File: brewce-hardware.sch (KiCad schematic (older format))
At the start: 18 parts, among them P1 CONN_I, P2 CONN_O, Q1 Q_NMOS_DGS, Q2 Q_NMOS_DGS, Q3 Q_NMOS_DGS, U1 MCP1700-3302E_TO92

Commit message: update schematics & PCB
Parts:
- added P3: CONN_DS18B20, Connect:bornier3, symbol CONN_01X03
- added R10: 4.7k, Resistors_ThroughHole:Resistor_Horizontal_RM10mm, symbol R
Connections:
- net GND: now also P3.1 (P1)
- net VDD: now also P3.3 (P3), R10.2
- new net: P3.2 (P2), R10.1
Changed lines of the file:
@@
 Wire Wire Line
 	2100 3200 2100 3000
+$Comp
+L CONN_01X03 P3
+U 1 1 5A0C64D8
+P 8550 5000
+F 0 "P3" H 8550 5200 50  0000 C CNN
+F 1 "CONN_DS18B20" V 8650 5000 50  0000 C CNN
+F 2 "Connect:bornier3" H 8550 5000 50  0001 C CNN
+F 3 "" H 8550 5000 50  0000 C CNN
+	1    8550 5000
+	1    0    0    1
+$EndComp
+$Comp
+L GND #PWR016
+U 1 1 5A0C682F
+P 8300 5250
+F 0 "#PWR016" H 8300 5000 50  0001 C CNN
+F 1 "GND" H 8300 5100 50  0000 C CNN
+F 2 "" H 8300 5250 50  0001 C CNN
+F 3 "" H 8300 5250 50  0001 C CNN
+	1    8300 5250
+	1    0    0    -1
+$EndComp
+Wire Wire Line
+	8350 5100 8300 5100
+Wire Wire Line
+	8300 5100 8300 5250
+$Comp
+L VDD #PWR017
+U 1 1 5A0C6B13
+P 8300 4500
+F 0 "#PWR017" H 8300 4350 50  0001 C CNN
+F 1 "VDD" H 8300 4650 50  0000 C CNN
+F 2 "" H 8300 4500 50  0001 C CNN
+F 3 "" H 8300 4500 50  0001 C CNN
+	1    8300 4500
+	1    0    0    -1
+$EndComp
+Wire Wire Line
+	8300 4900 8350 4900
+Wire Wire Line
+	8300 4500 8300 4900
+$Comp
+L R R10
+U 1 1 5A0C6C12
+P 8100 4800
+F 0 "R10" V 8180 4800 50  0000 C CNN
+F 1 "4.7k" V 8100 4800 50  0000 C CNN
+F 2 "Resistors_ThroughHole:Resistor_Horizontal_RM10mm" V 8030 4800 50  0001 C CNN
+F 3 "" H 8100 4800 50  0001 C CNN
+	1    8100 4800
+	-1   0    0    1
+$EndComp
+Wire Wire Line
+	8300 4600 8100 4600
+Wire Wire Line
+	8100 4600 8100 4650
+Connection ~ 8300 4600
+Wire Wire Line
+	8100 4950 8100 5000
+Wire Wire Line
+	8100 5000 8350 5000
 $EndSCHEMATC

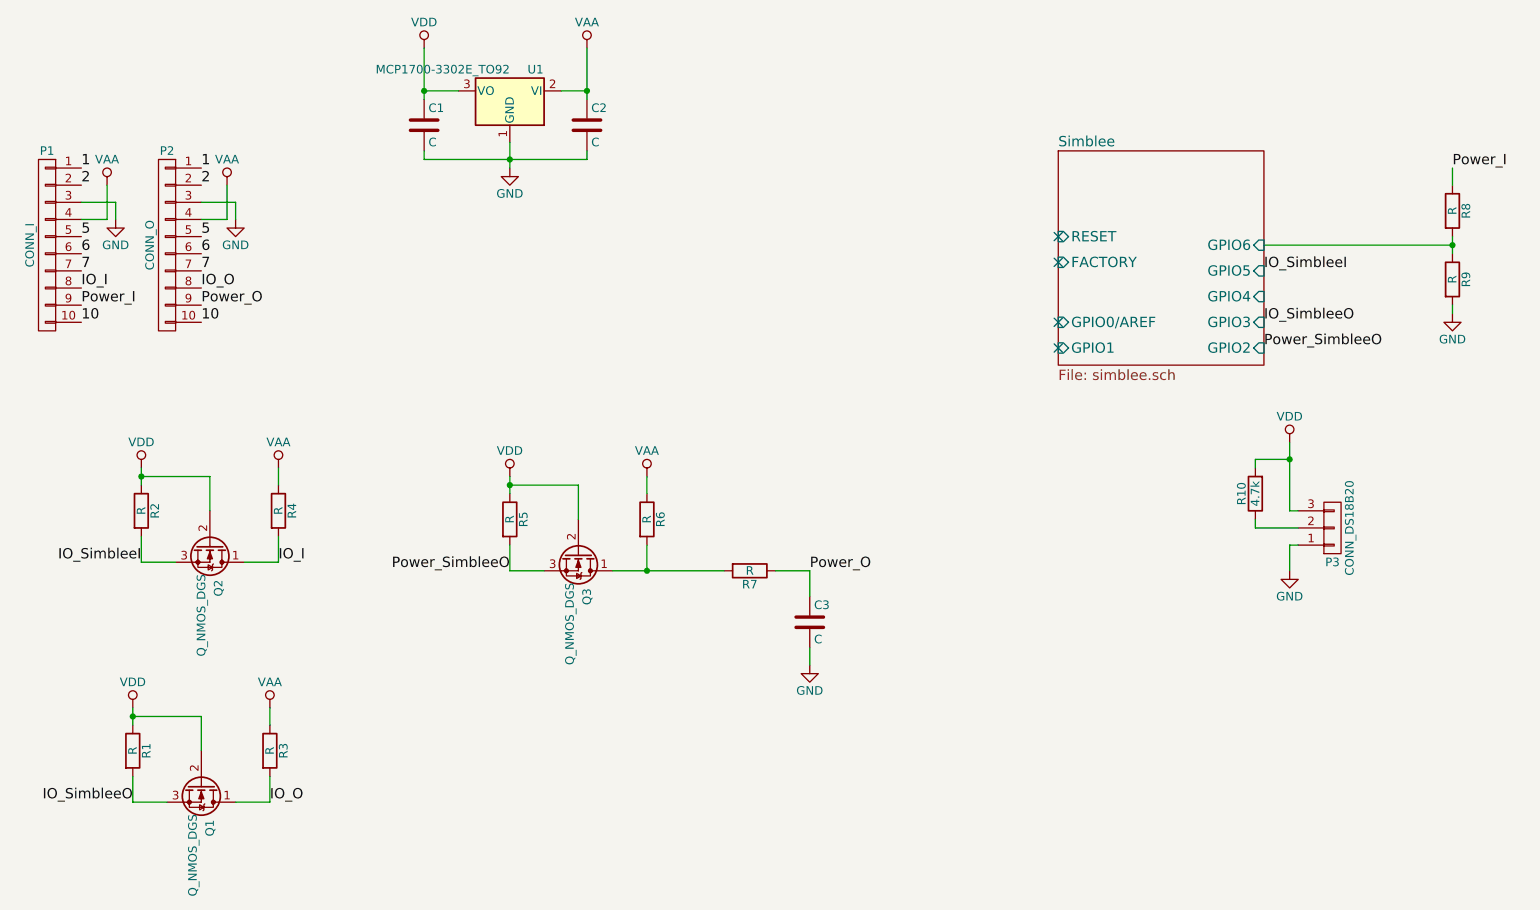
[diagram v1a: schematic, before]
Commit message: fix some problems in the schematics
- IO input read, use pull down instead of pull up
- PWM output to get all the values from 0 .. VAA for power output
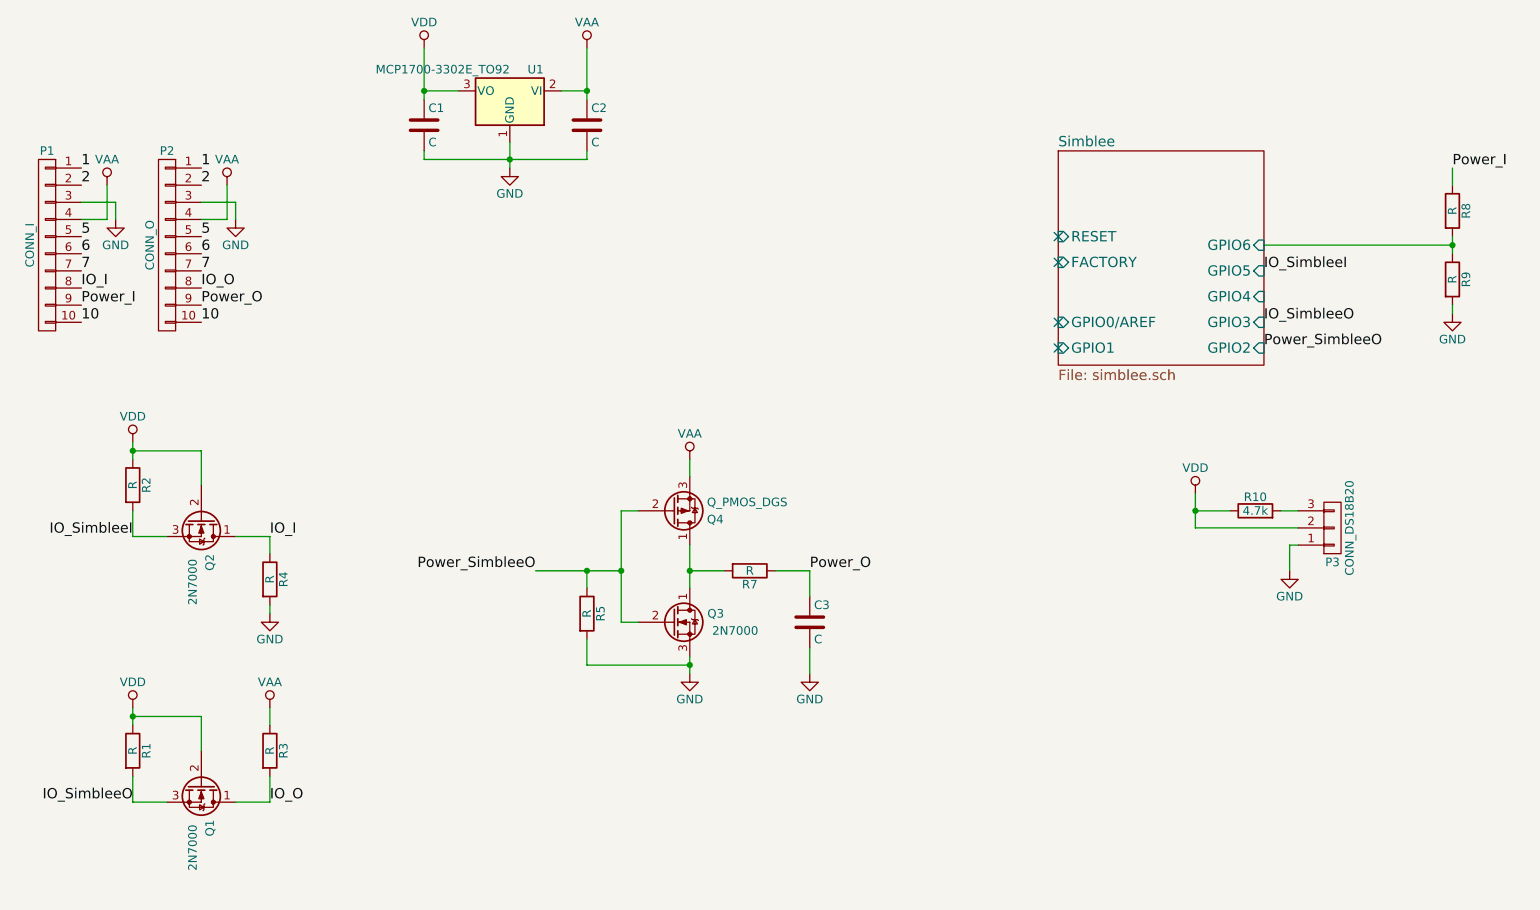
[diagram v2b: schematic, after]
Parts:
- removed R6: R, Resistors_ThroughHole:Resistor_Horizontal_RM10mm, symbol R
- added Q4: Q_PMOS_DGS, TO_SOT_Packages_THT:TO-92_Rugged, symbol Q_PMOS_DGS
- Q1, Q2, Q3: value Q_NMOS_DGS -> 2N7000; footprint TO_SOT_Packages_THT:TO-92_Inline_Narrow_Oval -> TO_SOT_Packages_THT:TO-92_Rugged
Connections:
- net GND: now also Q3.3 (S), R4.2, R5.2
- net IO_I: now also R4.1; no longer R4.2
- net Power_SimbleeO: now also Q3.2 (G), R5.1, Q4.2 (G); no longer Q3.3 (S), R5.2
- net VAA: now also Q4.3 (S); no longer R4.1
- net VDD: now also P3.2 (P2), R10.1; no longer P3.3 (P3), Q3.2 (G), R10.2, R5.1
- net at Q3.1 (D), R7.2: now also Q4.1 (D)
- new net: P3.3 (P3), R10.2
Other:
- moved on the sheet: Q2, Q3, R10, R2, R4, R5

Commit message: improve schematics, update pcb
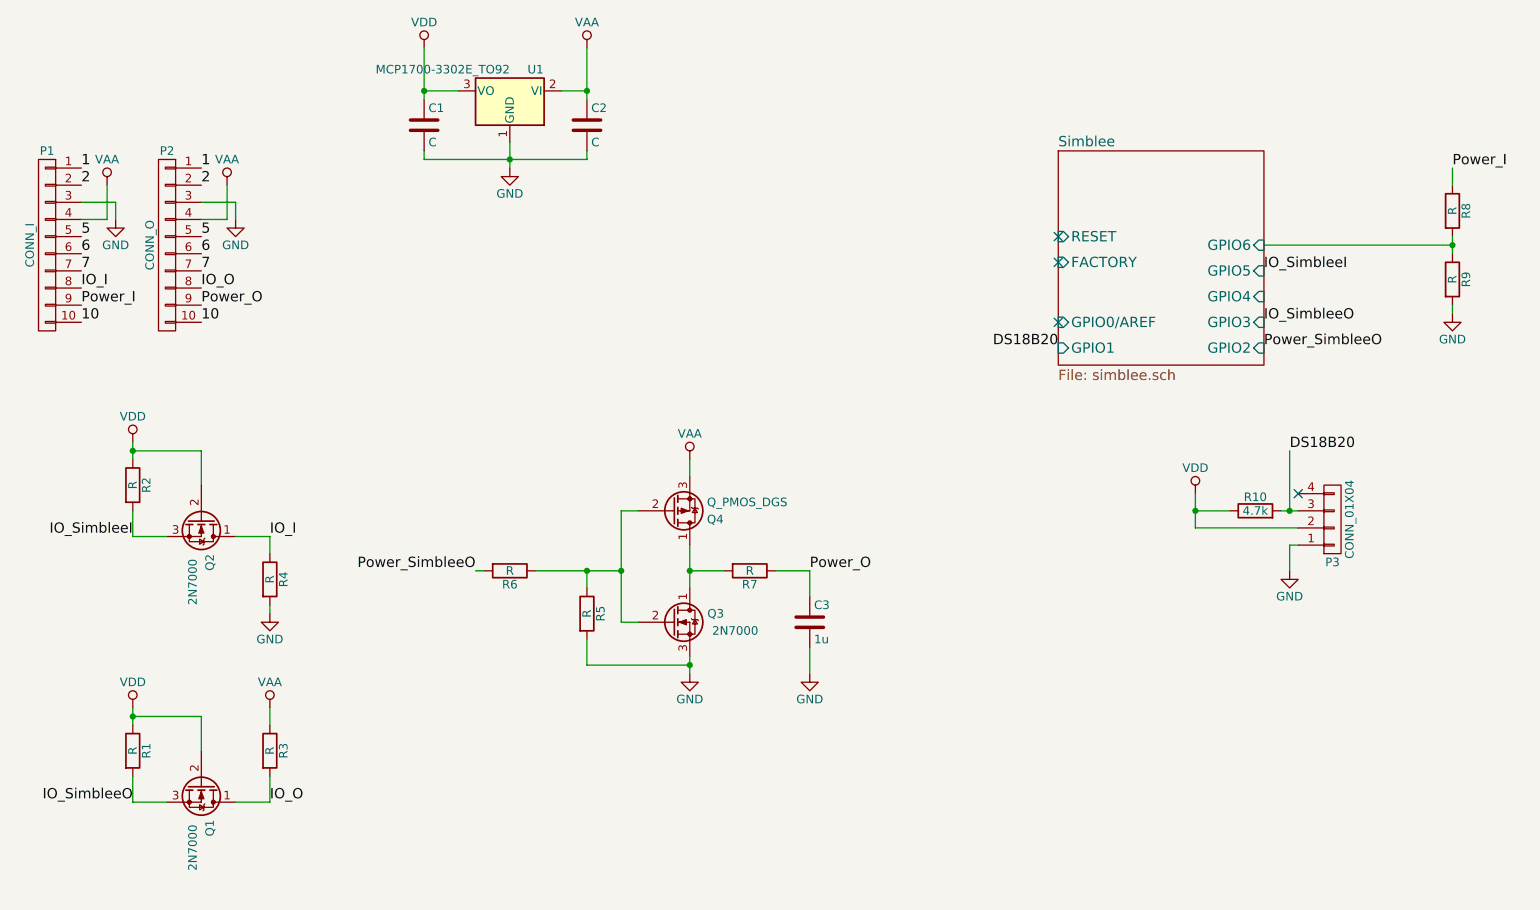
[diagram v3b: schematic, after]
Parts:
- removed P3: CONN_DS18B20, Connect:bornier3, symbol CONN_01X03
- added P3: CONN_01X04, Connect:bornier4, symbol CONN_01X04
- added R6: R, Resistors_ThroughHole:Resistor_Horizontal_RM10mm, symbol R
- C3: value C -> 1u
- U1: footprint TO_SOT_Packages_THT:TO-92_Inline_Narrow_Oval -> TO_SOT_Packages_THT:TO-92_Rugged
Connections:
- net GND: now also P3.1 (P1)
- net Power_SimbleeO: now also R6.2; no longer Q3.2 (G), Q4.2 (G), R5.1
- net VDD: now also P3.2 (P2)
- net DS18B20: now reaches R10.2
- net DS18B20: now also P3.3 (P3)
- new net: Q3.2 (G), Q4.2 (G), R5.1, R6.1
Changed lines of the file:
@@
 F 0 "U1" H 3600 2325 50  0000 C CNN
 F 1 "MCP1700-3302E_TO92" H 3750 2325 50  0000 L CNN
-F 2 "TO_SOT_Packages_THT:TO-92_Inline_Narrow_Oval" H 3750 2250 50  0001 C CIN
+F 2 "TO_SOT_Packages_THT:TO-92_Rugged" H 3750 2250 50  0001 C CIN
 F 3 "" H 3750 2450 50  0001 C CNN
 	1    3750 2450
@@
 P 5500 5550
 F 0 "C3" H 5525 5650 50  0000 L CNN
-F 1 "C" H 5525 5450 50  0000 L CNN
+F 1 "1u" H 5525 5450 50  0000 L CNN
 F 2 "Capacitors_ThroughHole:C_Rect_L7_W2_P5" H 5538 5400 50  0001 C CNN
 F 3 "" H 5500 5550 50  0001 C CNN
@@
 $EndComp
 $Comp
-L GND #PWR08
+L GND #PWR07
 U 1 1 5A0A0457
 P 5500 5850
-F 0 "#PWR08" H 5500 5600 50  0001 C CNN
+F 0 "#PWR07" H 5500 5600 50  0001 C CNN
 F 1 "GND" H 5500 5700 50  0000 C CNN
 F 2 "" H 5500 5850 50  0001 C CNN
@@
 	2350 6600 2350 6450
 $Comp
-L VDD #PWR09
+L VDD #PWR08
 U 1 1 5A0A3210
 P 1550 6050
-F 0 "#PWR09" H 1550 5900 50  0001 C CNN
+F 0 "#PWR08" H 1550 5900 50  0001 C CNN
 F 1 "VDD" H 1550 6200 50  0000 C CNN
 F 2 "" H 1550 6050 50  0001 C CNN
@@
 	1550 6050 1550 6150
 $Comp
-L VAA #PWR010
+L VAA #PWR09
 U 1 1 5A0A3217
 P 2350 6050
-F 0 "#PWR010" H 2350 5900 50  0001 C CNN
+F 0 "#PWR09" H 2350 5900 50  0001 C CNN
 F 1 "VAA" H 2350 6200 50  0000 C CNN
 F 2 "" H 2350 6050 50  0001 C CNN
@@
 NoConn ~ 6950 3300
 NoConn ~ 6950 3800
-NoConn ~ 6950 3950
 Text Label 8150 3950 0    60   ~ 0
 Power_SimbleeO
-Text Label 3900 5250 2    60   ~ 0
+Text Label 3550 5250 2    60   ~ 0
 Power_SimbleeO
 $Comp
-L GND #PWR011
+L GND #PWR010
 U 1 1 5A0A4243
 P 2150 3200
-F 0 "#PWR011" H 2150 2950 50  0001 C CNN
+F 0 "#PWR010" H 2150 2950 50  0001 C CNN
 F 1 "GND" H 2150 3050 50  0000 C CNN
 F 2 "" H 2150 3200 50  0001 C CNN
@@
 2
 $Comp
-L GND #PWR012
+L GND #PWR011
 U 1 1 5A0A45E0
 P 1450 3200
-F 0 "#PWR012" H 1450 2950 50  0001 C CNN
+F 0 "#PWR011" H 1450 2950 50  0001 C CNN
 F 1 "GND" H 1450 3050 50  0000 C CNN
 F 2 "" H 1450 3200 50  0001 C CNN
@@
 	1450 3100 1450 3200
 $Comp
-L VAA #PWR013
+L VAA #PWR012
 U 1 1 5A0A473E
 P 1400 3000
-F 0 "#PWR013" H 1400 2850 50  0001 C CNN
+F 0 "#PWR012" H 1400 2850 50  0001 C CNN
 F 1 "VAA" H 1400 3150 50  0000 C CNN
 F 2 "" H 1400 3000 50  0001 C CNN
@@
 	1400 3200 1400 3000
 $Comp
-L VAA #PWR014
+L VAA #PWR013
 U 1 1 5A0A4A33
 P 2100 3000
-F 0 "#PWR014" H 2100 2850 50  0001 C CNN
+F 0 "#PWR013" H 2100 2850 50  0001 C CNN
 F 1 "VAA" H 2100 3150 50  0000 C CNN
 F 2 "" H 2100 3000 50  0001 C CNN
@@
 	2100 3200 2100 3000
 $Comp
-L CONN_01X03 P3
-U 1 1 5A0C64D8
-P 8550 5000
-F 0 "P3" H 8550 5200 50  0000 C CNN
-F 1 "CONN_DS18B20" V 8650 5000 50  0000 C CNN
-F 2 "Connect:bornier3" H 8550 5000 50  0001 C CNN
-F 3 "" H 8550 5000 50  0000 C CNN
-	1    8550 5000
-	1    0    0    1
-$EndComp
-$Comp
-L GND #PWR015
+L GND #PWR014
 U 1 1 5A0C682F
 P 8300 5250
-F 0 "#PWR015" H 8300 5000 50  0001 C CNN
+F 0 "#PWR014" H 8300 5000 50  0001 C CNN
 F 1 "GND" H 8300 5100 50  0000 C CNN
 F 2 "" H 8300 5250 50  0001 C CNN
@@
 	8300 5100 8300 5250
 $Comp
-L VDD #PWR016
+L VDD #PWR015
 U 1 1 5A0C6B13
 P 7750 4800
-F 0 "#PWR016" H 7750 4650 50  0001 C CNN
+F 0 "#PWR015" H 7750 4650 50  0001 C CNN
 F 1 "VDD" H 7750 4950 50  0000 C CNN
 F 2 "" H 7750 4800 50  0001 C CNN
@@
 	4800 5100 4800 5350
 $Comp
-L GND #PWR017
+L GND #PWR016
 U 1 1 5A0EF370
 P 4800 5850
-F 0 "#PWR017" H 4800 5600 50  0001 C CNN
+F 0 "#PWR016" H 4800 5600 50  0001 C CNN
 F 1 "GND" H 4800 5700 50  0000 C CNN
 F 2 "" H 4800 5850 50  0001 C CNN
@@
 	2350 5050 2350 5150
 $Comp
-L GND #PWR?
+L GND #PWR017
 U 1 1 5A0F13A6
 P 2350 5500
-F 0 "#PWR?" H 2350 5250 50  0001 C CNN
+F 0 "#PWR017" H 2350 5250 50  0001 C CNN
 F 1 "GND" H 2350 5350 50  0000 C CNN
 F 2 "" H 2350 5500 50  0001 C CNN
@@
 Wire Wire Line
 	2350 5450 2350 5500
+$Comp
+L R R6
+U 1 1 5A16F5A3
+P 3750 5250
+F 0 "R6" V 3830 5250 50  0000 C CNN
+F 1 "R" V 3750 5250 50  0000 C CNN
+F 2 "Resistors_ThroughHole:Resistor_Horizontal_RM10mm" V 3680 5250 50  0001 C CNN
+F 3 "" H 3750 5250 50  0001 C CNN
+	1    3750 5250
+	0    1    1    0
+$EndComp
+Wire Wire Line
+	3600 5250 3550 5250
+$Comp
+L CONN_01X04 P3
+U 1 1 5A1E6679
+P 8550 4950
+F 0 "P3" H 8550 5200 50  0000 C CNN
+F 1 "CONN_01X04" V 8650 4950 50  0000 C CNN
+F 2 "Connect:bornier4" H 8550 4950 50  0001 C CNN
+F 3 "" H 8550 4950 50  0000 C CNN
+	1    8550 4950
+	1    0    0    1
+$EndComp
+NoConn ~ 8350 4800
+Wire Wire Line
+	8300 4900 8300 4550
+Connection ~ 8300 4900
+Text Label 8300 4550 0    60   ~ 0
+DS18B20
+Text Label 6950 3950 2    60   ~ 0
+DS18B20
 $EndSCHEMATC

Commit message: fix pwm level shifter
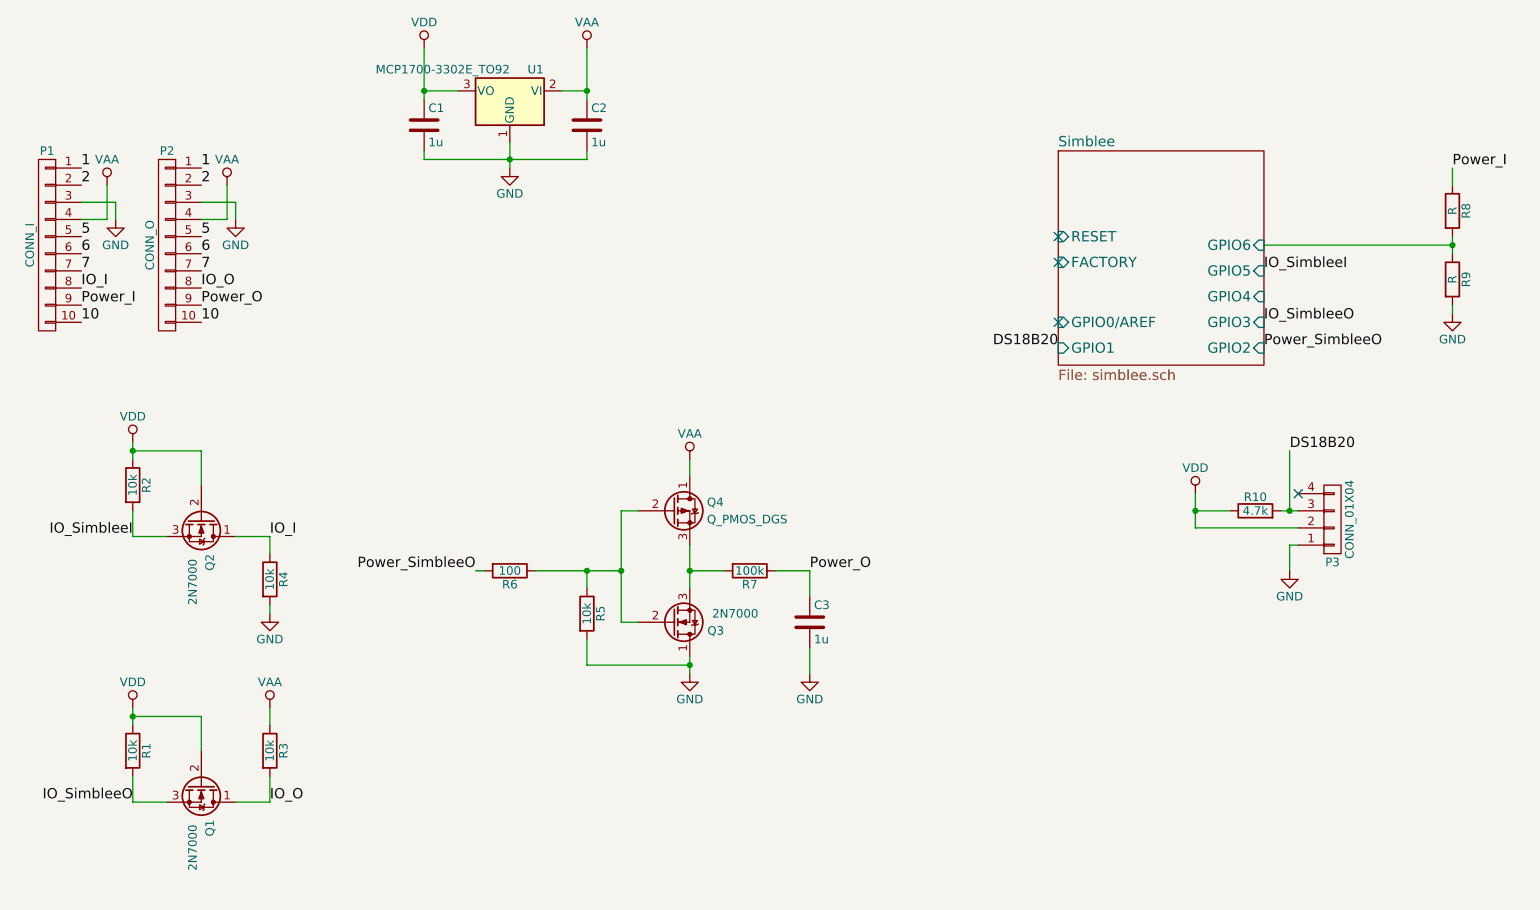
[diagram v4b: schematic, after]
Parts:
- C1, C2: value C -> 1u
- R1, R2, R3, R4, R5: value R -> 10k
- R6: value R -> 100
- R7: value R -> 100k
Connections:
- net GND: now also Q3.1 (D); no longer Q3.3 (S)
- net VAA: now also Q4.1 (D); no longer Q4.3 (S)
- new net: Q3.3 (S), Q4.3 (S), R7.2
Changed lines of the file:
@@
 F 3 "" H 4700 5550 50  0000 C CNN
 	1    4700 5550
-	1    0    0    -1
+	1    0    0    1
 $EndComp
 $Sheet
@@
 P 3250 2650
 F 0 "C1" H 3275 2750 50  0000 L CNN
-F 1 "C" H 3275 2550 50  0000 L CNN
+F 1 "1u" H 3275 2550 50  0000 L CNN
 F 2 "Capacitors_ThroughHole:C_Rect_L7_W2_P5" H 3288 2500 50  0001 C CNN
 F 3 "" H 3250 2650 50  0001 C CNN
@@
 P 4200 2650
 F 0 "C2" H 4225 2750 50  0000 L CNN
-F 1 "C" H 4225 2550 50  0000 L CNN
+F 1 "1u" H 4225 2550 50  0000 L CNN
 F 2 "Capacitors_ThroughHole:C_Rect_L7_W2_P5" H 4238 2500 50  0001 C CNN
 F 3 "" H 4200 2650 50  0001 C CNN
@@
 P 4200 5500
 F 0 "R5" V 4280 5500 50  0000 C CNN
-F 1 "R" V 4200 5500 50  0000 C CNN
+F 1 "10k" V 4200 5500 50  0000 C CNN
 F 2 "Resistors_ThroughHole:Resistor_Horizontal_RM10mm" V 4130 5500 50  0001 C CNN
 F 3 "" H 4200 5500 50  0001 C CNN
@@
 P 1550 4750
 F 0 "R2" V 1630 4750 50  0000 C CNN
-F 1 "R" V 1550 4750 50  0000 C CNN
+F 1 "10k" V 1550 4750 50  0000 C CNN
 F 2 "Resistors_ThroughHole:Resistor_Horizontal_RM10mm" V 1480 4750 50  0001 C CNN
 F 3 "" H 1550 4750 50  0001 C CNN
@@
 P 2350 5300
 F 0 "R4" V 2430 5300 50  0000 C CNN
-F 1 "R" V 2350 5300 50  0000 C CNN
+F 1 "10k" V 2350 5300 50  0000 C CNN
 F 2 "Resistors_ThroughHole:Resistor_Horizontal_RM10mm" V 2280 5300 50  0001 C CNN
 F 3 "" H 2350 5300 50  0001 C CNN
@@
 P 5150 5250
 F 0 "R7" V 5230 5250 50  0000 C CNN
-F 1 "R" V 5150 5250 50  0000 C CNN
+F 1 "100k" V 5150 5250 50  0000 C CNN
 F 2 "Resistors_ThroughHole:Resistor_Horizontal_RM10mm" V 5080 5250 50  0001 C CNN
 F 3 "" H 5150 5250 50  0001 C CNN
@@
 P 1550 6300
 F 0 "R1" V 1630 6300 50  0000 C CNN
-F 1 "R" V 1550 6300 50  0000 C CNN
+F 1 "10k" V 1550 6300 50  0000 C CNN
 F 2 "Resistors_ThroughHole:Resistor_Horizontal_RM10mm" V 1480 6300 50  0001 C CNN
 F 3 "" H 1550 6300 50  0001 C CNN
@@
 P 2350 6300
 F 0 "R3" V 2430 6300 50  0000 C CNN
-F 1 "R" V 2350 6300 50  0000 C CNN
+F 1 "10k" V 2350 6300 50  0000 C CNN
 F 2 "Resistors_ThroughHole:Resistor_Horizontal_RM10mm" V 2280 6300 50  0001 C CNN
 F 3 "" H 2350 6300 50  0001 C CNN
@@
 F 3 "" H 4700 4900 50  0001 C CNN
 	1    4700 4900
-	1    0    0    1
+	1    0    0    -1
 $EndComp
 Connection ~ 4800 5250
@@
 P 3750 5250
 F 0 "R6" V 3830 5250 50  0000 C CNN
-F 1 "R" V 3750 5250 50  0000 C CNN
+F 1 "100" V 3750 5250 50  0000 C CNN
 F 2 "Resistors_ThroughHole:Resistor_Horizontal_RM10mm" V 3680 5250 50  0001 C CNN
 F 3 "" H 3750 5250 50  0001 C CNN
